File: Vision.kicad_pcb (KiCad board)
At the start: 2 copper layers, 299.2 x 124 mm, 145 parts, among them J1 Conn_ARM_JTAG_SWD_10, Q1 DTC123J, SW1 SW_Push, U1 MCP1700-3002E_SOT23, U2 STM32F072CBUx, U3 TPD4E05U06DQAR

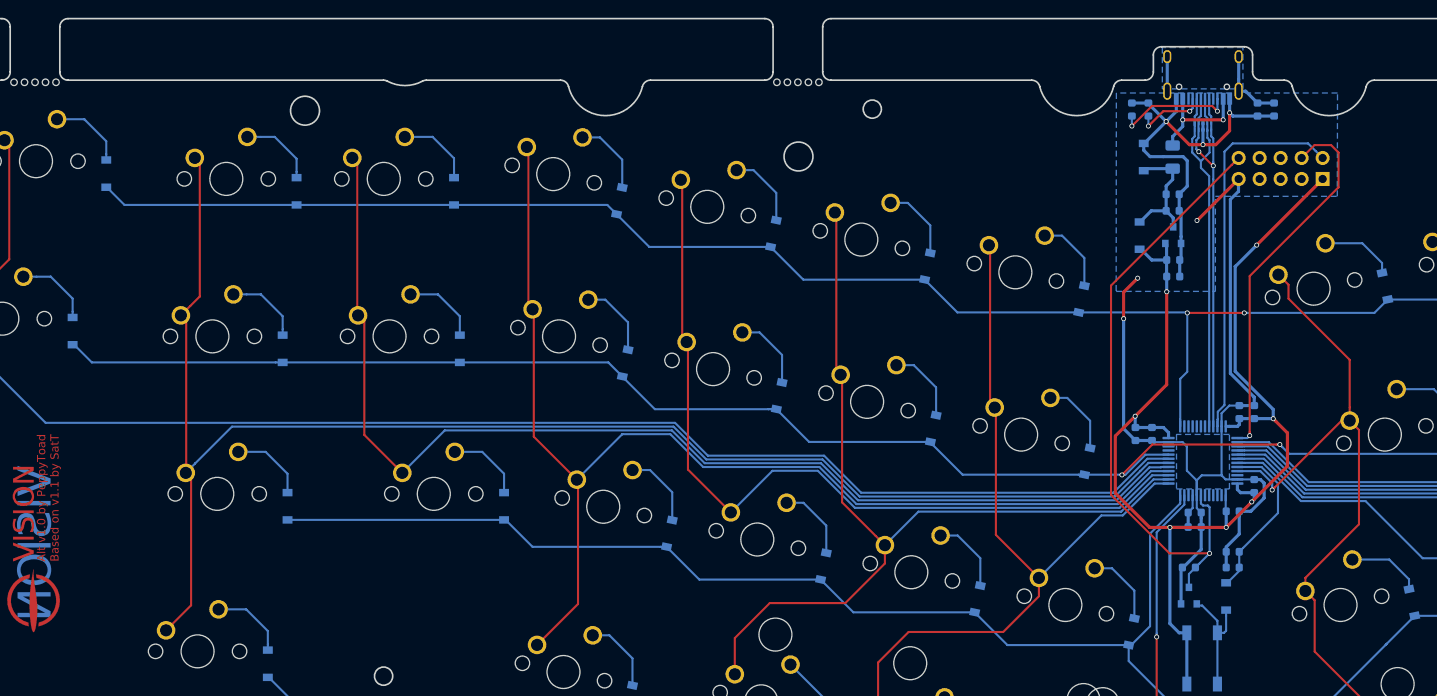
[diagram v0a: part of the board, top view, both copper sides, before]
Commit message: Use native Kicad USB-C footprint
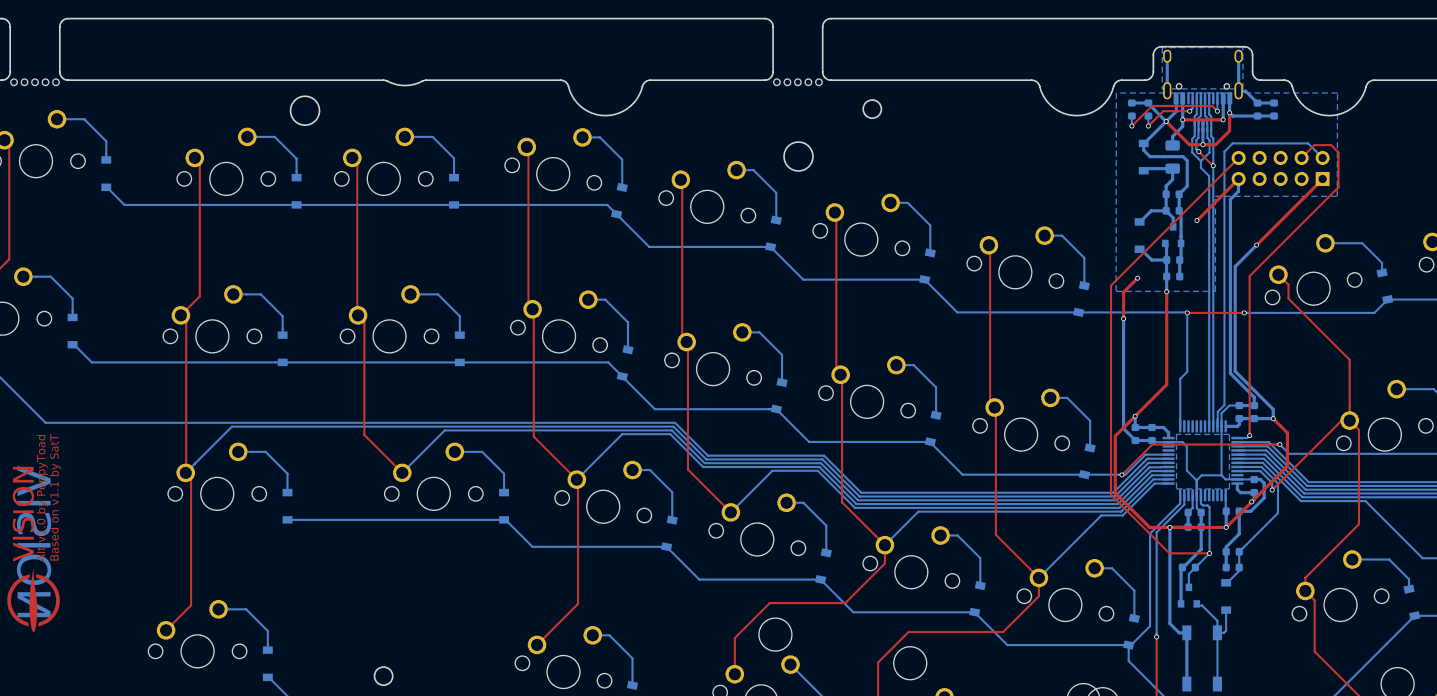
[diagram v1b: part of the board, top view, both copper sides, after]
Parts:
- USB1: footprint Type-C:HRO-TYPE-C-31-M-12-Assembly -> Connector_USB:USB_C_Receptacle_HRO_TYPE-C-31-M-12
- moved USB1 3.60 mm to (210.0, 83.6)
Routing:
- net GND: track 175.5 -> 174.9 mm

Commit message: Final pre-proto changes
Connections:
- USB1 pad S1: (no net) -> Net-(C3-Pad2)
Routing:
- net Net-(C3-Pad2): track 13.2 -> 21.9 mm
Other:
- board text added: "JLCJLCJLCJLC"
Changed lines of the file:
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@@
       (effects (font (size 1 1) (thickness 0.15)) (justify mirror))
     )
+    (fp_line (start -4.7 -2) (end -4.7 -3.9) (layer "B.SilkS") (width 0.12))
+    (fp_line (start 4.7 1.9) (end 4.7 -0.1) (layer "B.SilkS") (width 0.12))
     (fp_line (start -4.7 -3.9) (end 4.7 -3.9) (layer "B.SilkS") (width 0.12))
-    (fp_line (start 4.7 1.9) (end 4.7 -0.1) (layer "B.SilkS") (width 0.12))
     (fp_line (start 4.7 -2) (end 4.7 -3.9) (layer "B.SilkS") (width 0.12))
     (fp_line (start -4.7 1.9) (end -4.7 -0.1) (layer "B.SilkS") (width 0.12))
-    (fp_line (start -4.7 -2) (end -4.7 -3.9) (layer "B.SilkS") (width 0.12))
     (fp_line (start -5.32 -4.15) (end 5.32 -4.15) (layer "B.CrtYd") (width 0.05))
     (fp_line (start -5.32 5.27) (end 5.32 5.27) (layer "B.CrtYd") (width 0.05))
+    (fp_line (start 5.32 5.27) (end 5.32 -4.15) (layer "B.CrtYd") (width 0.05))
     (fp_line (start -5.32 5.27) (end -5.32 -4.15) (layer "B.CrtYd") (width 0.05))
-    (fp_line (start 5.32 5.27) (end 5.32 -4.15) (layer "B.CrtYd") (width 0.05))
+    (fp_line (start 4.47 3.65) (end 4.47 -3.65) (layer "B.Fab") (width 0.1))
+    (fp_line (start -4.47 3.65) (end -4.47 -3.65) (layer "B.Fab") (width 0.1))
     (fp_line (start -4.47 -3.65) (end 4.47 -3.65) (layer "B.Fab") (width 0.1))
-    (fp_line (start -4.47 3.65) (end -4.47 -3.65) (layer "B.Fab") (width 0.1))
-    (fp_line (start 4.47 3.65) (end 4.47 -3.65) (layer "B.Fab") (width 0.1))
     (fp_line (start -4.47 3.65) (end 4.47 3.65) (layer "B.Fab") (width 0.1))
+    (pad "" np_thru_hole circle (at 2.89 2.6) (size 0.65 0.65) (drill 0.65) (layers *.Cu *.Mask))
     (pad "" np_thru_hole circle (at -2.89 2.6) (size 0.65 0.65) (drill 0.65) (layers *.Cu *.Mask))
-    (pad "" np_thru_hole circle (at 2.89 2.6) (size 0.65 0.65) (drill 0.65) (layers *.Cu *.Mask))
     (pad "A1" smd rect (at -3.25 4.045) (size 0.6 1.45) (layers "B.Cu" "B.Paste" "B.Mask"))
     (pad "A4" smd rect (at -2.45 4.045) (size 0.6 1.45) (layers "B.Cu" "B.Paste" "B.Mask"))
@@
     (pad "B9" smd rect (at -2.45 4.045) (size 0.6 1.45) (layers "B.Cu" "B.Paste" "B.Mask"))
     (pad "B12" smd rect (at -3.25 4.045) (size 0.6 1.45) (layers "B.Cu" "B.Paste" "B.Mask"))
-    (pad "S1" thru_hole oval (at -4.32 3.13) (size 1 2.1) (drill oval 0.6 1.7) (layers *.Cu *.Mask))
-    (pad "S1" thru_hole oval (at 4.32 3.13) (size 1 2.1) (drill oval 0.6 1.7) (layers *.Cu *.Mask))
-    (pad "S1" thru_hole oval (at 4.32 -1.05) (size 1 1.6) (drill oval 0.6 1.2) (layers *.Cu *.Mask))
-    (pad "S1" thru_hole oval (at -4.32 -1.05) (size 1 1.6) (drill oval 0.6 1.2) (layers *.Cu *.Mask))
+    (pad "S1" thru_hole oval (at 4.32 -1.05) (size 1 1.6) (drill oval 0.6 1.2) (layers *.Cu *.Mask)
+      (net 55 "Net-(C3-Pad2)"))
+    (pad "S1" thru_hole oval (at -4.32 3.13) (size 1 2.1) (drill oval 0.6 1.7) (layers *.Cu *.Mask)
+      (net 55 "Net-(C3-Pad2)"))
+    (pad "S1" thru_hole oval (at -4.32 -1.05) (size 1 1.6) (drill oval 0.6 1.2) (layers *.Cu *.Mask)
+      (net 55 "Net-(C3-Pad2)"))
+    (pad "S1" thru_hole oval (at 4.32 3.13) (size 1 2.1) (drill oval 0.6 1.7) (layers *.Cu *.Mask)
+      (net 55 "Net-(C3-Pad2)"))
     (model "${KICAD6_3DMODEL_DIR}/Connector_USB.3dshapes/USB_C_Receptacle_HRO_TYPE-C-31-M-12.wrl"
       (offset (xyz 0 0 0))
@@
   (gr_text "VISION" (at 67.4 143.7 90) (layer "F.Cu")
     (effects (font (size 2.5 2.5) (thickness 0.2)) (justify left))
+  )
+  (gr_text "JLCJLCJLCJLC" (at 210 73.1) (layer "B.Cu")
+    (effects (font (size 1.5 1.5) (thickness 0.3)) (justify mirror))
   )
   (gr_text "GND" (at 221.9 99.7) (layer "B.SilkS")
@@
   (segment (start 212.6 94.1) (end 213.6 93.1) (width 0.254) (layer "B.Cu") (net 54))
   (segment (start 211.76979 127.308823) (end 211.769789 126.498267) (width 0.254) (layer "B.Cu") (net 54))
+  (segment (start 205.68 82.55) (end 214.32 82.55) (width 0.381) (layer "F.Cu") (net 55))
   (segment (start 214.32 85.349) (end 214.32 82.6) (width 0.381) (layer "B.Cu") (net 55))
   (segment (start 216.6 88.2125) (end 218.6 88.2125) (width 0.381) (layer "B.Cu") (net 55))
